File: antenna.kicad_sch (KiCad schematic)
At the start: 6 parts, among them J1 Conn_Coaxial, J2 Conn_Coaxial

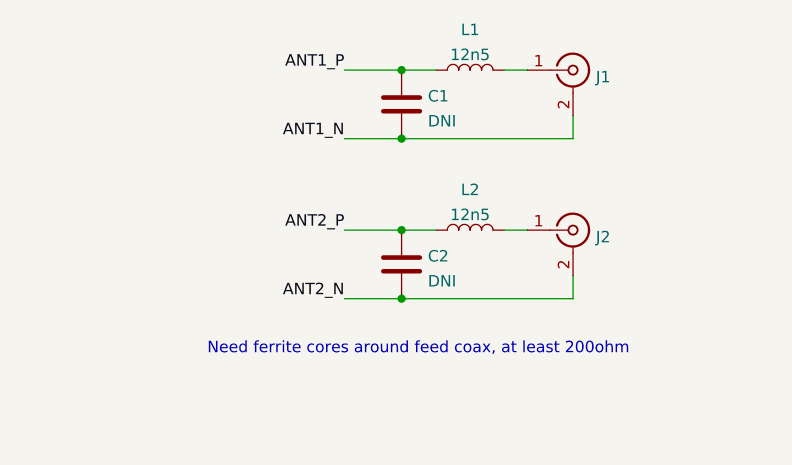
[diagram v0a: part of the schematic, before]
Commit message: Edit silkscreen and generate gerbers
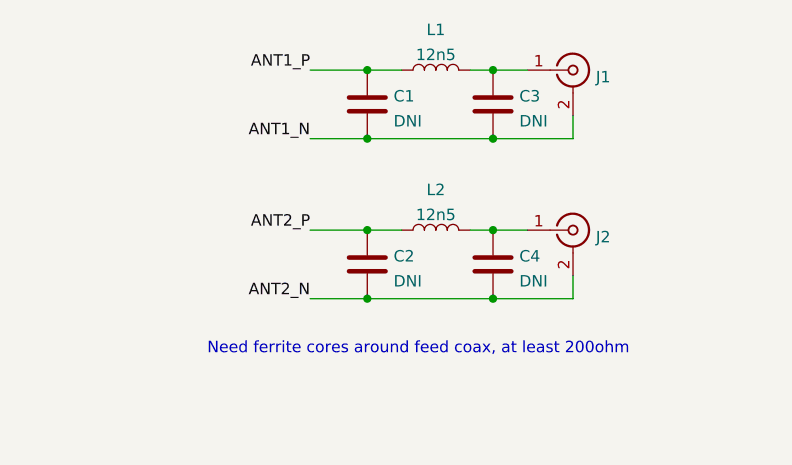
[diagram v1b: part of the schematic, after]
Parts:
- added C3, C4: DNI, Capacitor_SMD:C_0603_1608Metric_Pad1.08x0.95mm_HandSolder, symbol Device:C
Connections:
- net ANT1_N: now also C3.2
- net ANT2_N: now also C4.2
- net at J1.1 (In), L1.2: now also C3.1
- net at J2.1 (In), L2.2: now also C4.1
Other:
- moved on the sheet: C1, C2, L1, L2

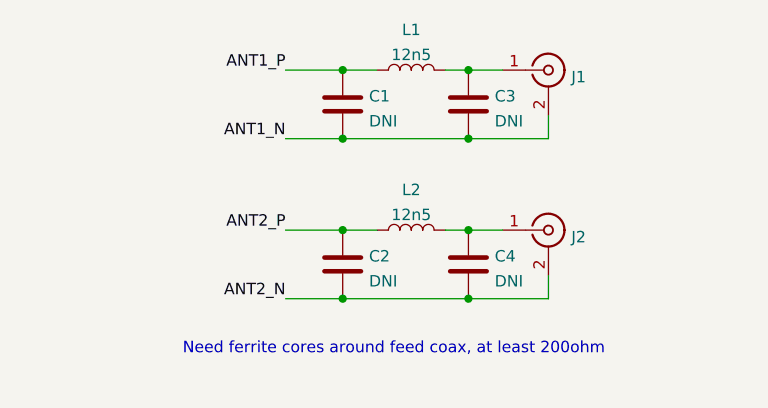
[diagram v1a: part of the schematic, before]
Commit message: Made Single Antenna
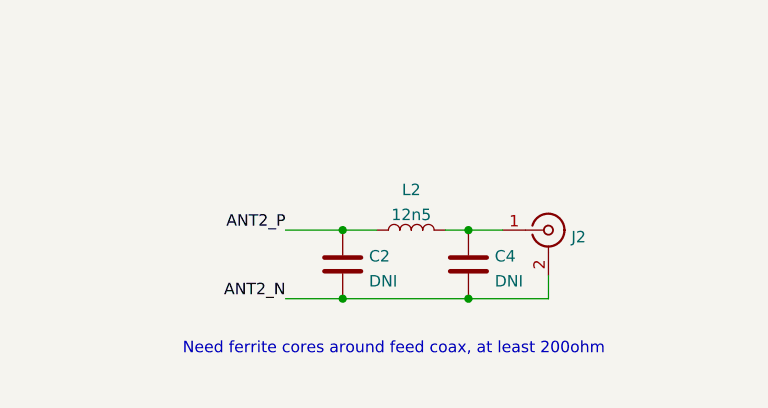
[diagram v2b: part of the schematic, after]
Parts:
- removed C1, C3: DNI, Capacitor_SMD:C_0603_1608Metric_Pad1.08x0.95mm_HandSolder, symbol Device:C
- removed J1: Conn_Coaxial, Connector_Coaxial:SMB_Jack_Vertical, symbol Connector:Conn_Coaxial
- removed L1: 12n5, Inductor_SMD:L_0603_1608Metric_Pad1.05x0.95mm_HandSolder, symbol Device:L
